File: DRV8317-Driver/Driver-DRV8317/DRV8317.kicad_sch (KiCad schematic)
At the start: 19 parts, among them IC3 DRV8317HREER, J1 Conn_02x13_Odd_Even, J6 Screw_Terminal_01x03

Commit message: kncoadsnofijasndvoi
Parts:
- R42: footprint Resistor_SMD:R_0603_1608Metric -> Resistor_SMD:R_0805_2012Metric
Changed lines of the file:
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@@
 	(wire
 		(pts
-			(xy 153.67 93.98) (xy 158.75 93.98)
+			(xy 95.25 93.98) (xy 100.33 93.98)
 		)
 		(stroke
@@
 	(wire
 		(pts
-			(xy 158.75 93.98) (xy 158.75 90.17)
+			(xy 100.33 93.98) (xy 100.33 90.17)
 		)
 		(stroke
@@
 	(global_label "AVDD"
 		(shape input)
-		(at 153.67 93.98 180)
+		(at 95.25 93.98 180)
 		(fields_autoplaced yes)
 		(effects
@@
 		)
 		(property "Intersheetrefs" "${INTERSHEET_REFS}"
-			(at 146.047 93.98 0)
+			(at 87.627 93.98 0)
 			(effects
 				(font
@@
 			)
 		)
-		(property "Footprint" "Resistor_SMD:R_0603_1608Metric"
+		(property "Footprint" "Resistor_SMD:R_0805_2012Metric"
 			(at 206.248 41.91 90)
 			(effects
@@
 	(symbol
 		(lib_id "power:+3.3V")
-		(at 158.75 90.17 0)
+		(at 100.33 90.17 0)
 		(unit 1)
 		(exclude_from_sim no)
@@
 		(fields_autoplaced yes)
 		(property "Reference" "#PWR051"
-			(at 158.75 93.98 0)
+			(at 100.33 93.98 0)
 			(effects
 				(font
@@
 		)
 		(property "Value" "+3.3V"
-			(at 158.75 85.09 0)
+			(at 100.33 85.09 0)
 			(effects
 				(font
@@
 		)
 		(property "Footprint" ""
-			(at 158.75 90.17 0)
+			(at 100.33 90.17 0)
 			(effects
 				(font
@@
 		)
 		(property "Datasheet" ""
-			(at 158.75 90.17 0)
+			(at 100.33 90.17 0)
 			(effects
 				(font
@@
 		)
 		(property "Description" ""
-			(at 158.75 90.17 0)
+			(at 100.33 90.17 0)
 			(effects
 				(font

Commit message: Up
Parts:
- added C33, C34, C35: 22pF, Capacitor_SMD:C_0603_1608Metric, symbol Device:C
- added D6: Red LED, LED_SMD:LED_0805_2012Metric, symbol Device:LED
- added R36, R37: 3.6, Resistor_SMD:R_0805_2012Metric, symbol Device:R
- added R4, R5, R6: 330, Resistor_SMD:R_0603_1608Metric, symbol Device:R
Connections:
- net GND: now also C33.1, C34.1, C35.1, D6.1 (K)
- net NFAULT: now also R36.1
- net Vcurrfdbk_A: now also R4.1; no longer J1.5 (Pin_5)
- net Vcurrfdbk_B: now also R5.1; no longer J1.7 (Pin_7)
- net Vcurrfdbk_C: now also R6.1; no longer J1.9 (Pin_9)
- new net: C33.2, J1.5 (Pin_5), R4.2
- new net: R36.2, R37.1
- new net: D6.2 (A), R37.2
- new net: C35.2, J1.9 (Pin_9), R6.2
- new net: C34.2, J1.7 (Pin_7), R5.2
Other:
- moved on the sheet: J1, J6

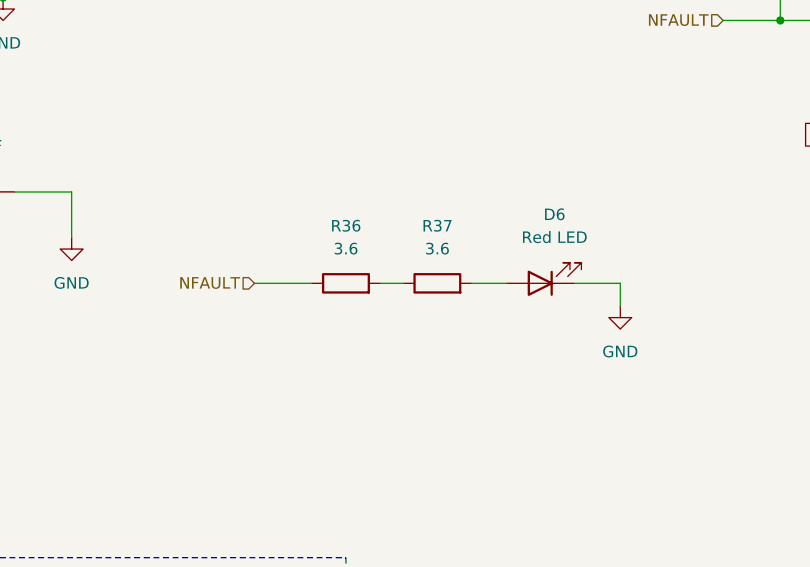
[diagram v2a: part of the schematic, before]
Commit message: fix all via to 0.45/0.3 mm
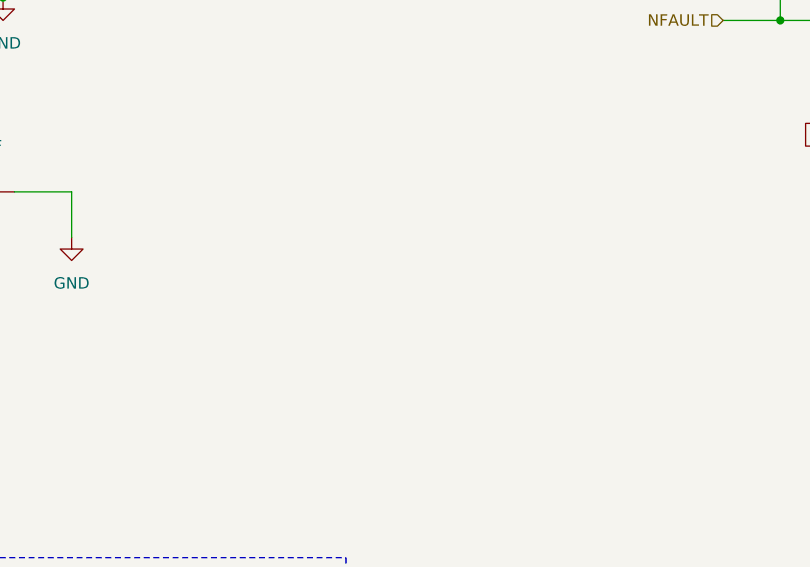
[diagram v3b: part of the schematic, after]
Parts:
- removed D6: Red LED, LED_SMD:LED_0805_2012Metric, symbol Device:LED
- removed R36, R37: 3.6, Resistor_SMD:R_0805_2012Metric, symbol Device:R
